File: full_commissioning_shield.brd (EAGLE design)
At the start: 140 x 53.3 mm, 118 parts, among them IC1 LSM303DLHC, IC2 TLV341A, Q1 BSS138, Q2 BSS138, Q3 NMOS BSS138, U1 ARDUINO-MEGAPRO-5V, U10 LM3405XMK, U11 DS1342U+, U13 TPS563200, U14 MIC5365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

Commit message: Fixed some errors
- Fixed a missing net
- Minor polygon fixes
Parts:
- R35: value 680k -> 580k
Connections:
- net LIGHT_PWM: now also U1.45
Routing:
- net LIGHT_PWM: track 9.08 -> 81.7 mm, vias 2 -> 3
- net SCL_3V3: track 103.5 -> 104.8 mm, vias 6 -> 5
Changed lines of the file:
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@@
 <attribute name="VALUE" x="44.7675" y="18.7325" size="1.27" layer="27"/>
 </element>
-<element name="R35" library="rcl" package="R0805" value="680k" x="45.4025" y="17.4625" smashed="yes" rot="R180">
+<element name="R35" library="rcl" package="R0805" value="580k" x="45.4025" y="17.4625" smashed="yes" rot="R180">
 <attribute name="NAME" x="42.8625" y="18.0975" size="0.8128" layer="25" rot="R270"/>
 <attribute name="VALUE" x="46.0375" y="20.0025" size="1.27" layer="27" rot="R180"/>
@@
 </element>
 <element name="C31" library="rcl" package="C0805" value="100n" x="40.9575" y="15.5575" smashed="yes" rot="R180">
-<attribute name="NAME" x="38.4175" y="16.1925" size="0.8128" layer="25" rot="R270"/>
+<attribute name="NAME" x="38.4175" y="15.875" size="0.8128" layer="25" rot="R270"/>
 <attribute name="VALUE" x="42.2275" y="18.0975" size="1.27" layer="27" rot="R180"/>
 </element>
@@
 <vertex x="27.445" y="41.25"/>
 <vertex x="21.215" y="41.25"/>
-<vertex x="21.215" y="39.6875"/>
-<vertex x="11.155" y="39.6875"/>
-<vertex x="11.155" y="45.2525"/>
-<vertex x="9.0225" y="45.2525"/>
+<vertex x="21.215" y="40.005"/>
+<vertex x="10.8375" y="40.005"/>
+<vertex x="10.8375" y="45.57"/>
+<vertex x="9.0225" y="45.57"/>
 <vertex x="9.0225" y="40.3125"/>
 <vertex x="8.9975" y="40.3125"/>
@@
 <contactref element="U10" pad="5"/>
 <contactref element="C23" pad="2"/>
-<polygon width="0.254" layer="1">
+<polygon width="0.254" layer="1" thermals="no">
 <vertex x="20.0075" y="19.9875"/>
 <vertex x="22.7925" y="19.9875"/>
@@
 <contactref element="C7" pad="1"/>
 <contactref element="R6" pad="2"/>
-<polygon width="0.254" layer="1" orphans="yes">
+<polygon width="0.254" layer="1" orphans="yes" thermals="no">
 <vertex x="18.13" y="49.6975"/>
 <vertex x="30.2775" y="49.6975"/>
@@
 <wire x1="20.3073" y1="25.6352" x2="20.3073" y2="24.5298" width="0.254" layer="1"/>
 <wire x1="20.3073" y1="24.5298" x2="20.2925" y2="24.515" width="0.254" layer="1"/>
+<contactref element="U1" pad="45"/>
+<wire x1="85.09" y1="20.32" x2="83.82" y2="19.05" width="0.3048" layer="16"/>
+<wire x1="83.82" y1="19.05" x2="40.9575" y2="19.05" width="0.3048" layer="16"/>
+<wire x1="40.9575" y1="19.05" x2="38.1" y2="16.1925" width="0.3048" layer="16"/>
+<wire x1="38.1" y1="16.1925" x2="28.8925" y2="16.1925" width="0.3048" layer="1"/>
+<wire x1="28.8925" y1="16.1925" x2="26.035" y2="19.05" width="0.3048" layer="1"/>
+<wire x1="26.035" y1="19.05" x2="18.7725" y2="19.05" width="0.3048" layer="1"/>
+<wire x1="18.7725" y1="19.05" x2="16.355" y2="21.4675" width="0.3048" layer="1"/>
+<via x="38.1" y="16.1925" extent="1-16" drill="0.35" diameter="0.1" shape="octagon"/>
 </signal>
 <signal name="N$19">
@@
 <contactref element="U10" pad="6"/>
 <contactref element="L2" pad="1"/>
-<polygon width="0.254" layer="1" rank="2">
+<polygon width="0.254" layer="1" thermals="no" rank="2">
 <vertex x="19.07" y="31.75"/>
 <vertex x="19.07" y="27.66"/>
@@
 <contactref element="L2" pad="2"/>
 <contactref element="LED" pad="1"/>
-<polygon width="0.4064" layer="1" isolate="0.3048">
+<polygon width="0.4064" layer="1" isolate="0.3048" thermals="no">
 <vertex x="15.9375" y="36.41"/>
 <vertex x="3.13" y="36.41"/>
@@
 <via x="12.7" y="25.7125" extent="1-16" drill="0.35" diameter="0.1" shape="octagon"/>
 <wire x1="12.66" y1="23.9695" x2="10.12" y2="23.9695" width="0.8128" layer="1"/>
-<polygon width="0.6096" layer="1">
+<polygon width="0.6096" layer="1" thermals="no">
 <vertex x="3.175" y="29.845"/>
 <vertex x="9.8425" y="29.845"/>
@@
 <vertex x="13.3825" y="40.625"/>
 </polygon>
-<polygon width="0.254" layer="1">
-<vertex x="11.82" y="45.3125"/>
-<vertex x="11.82" y="40.625"/>
+<polygon width="0.254" layer="1" thermals="no">
+<vertex x="11.5025" y="45.63"/>
+<vertex x="11.5025" y="40.625"/>
 <vertex x="13.07" y="40.625"/>
-<vertex x="13.07" y="45.3125"/>
+<vertex x="13.07" y="45.63"/>
 </polygon>
 <via x="12.445" y="42.1875" extent="1-16" drill="0.35" diameter="0.1" shape="octagon"/>
@@
 <wire x1="69.5325" y1="36.83" x2="68.8975" y2="37.465" width="0.254" layer="16"/>
 <contactref element="GPS" pad="14"/>
-<via x="67.5875" y="37.465" extent="1-16" drill="0.35" diameter="0.1" shape="octagon"/>
-<wire x1="67.5875" y1="37.465" x2="65.405" y2="37.465" width="0.254" layer="16"/>
+<wire x1="68.8975" y1="37.465" x2="65.405" y2="37.465" width="0.254" layer="16"/>
 <wire x1="65.405" y1="37.465" x2="63.5" y2="39.37" width="0.254" layer="16"/>
 <wire x1="63.5" y1="39.37" x2="63.5" y2="41.595" width="0.254" layer="16"/>

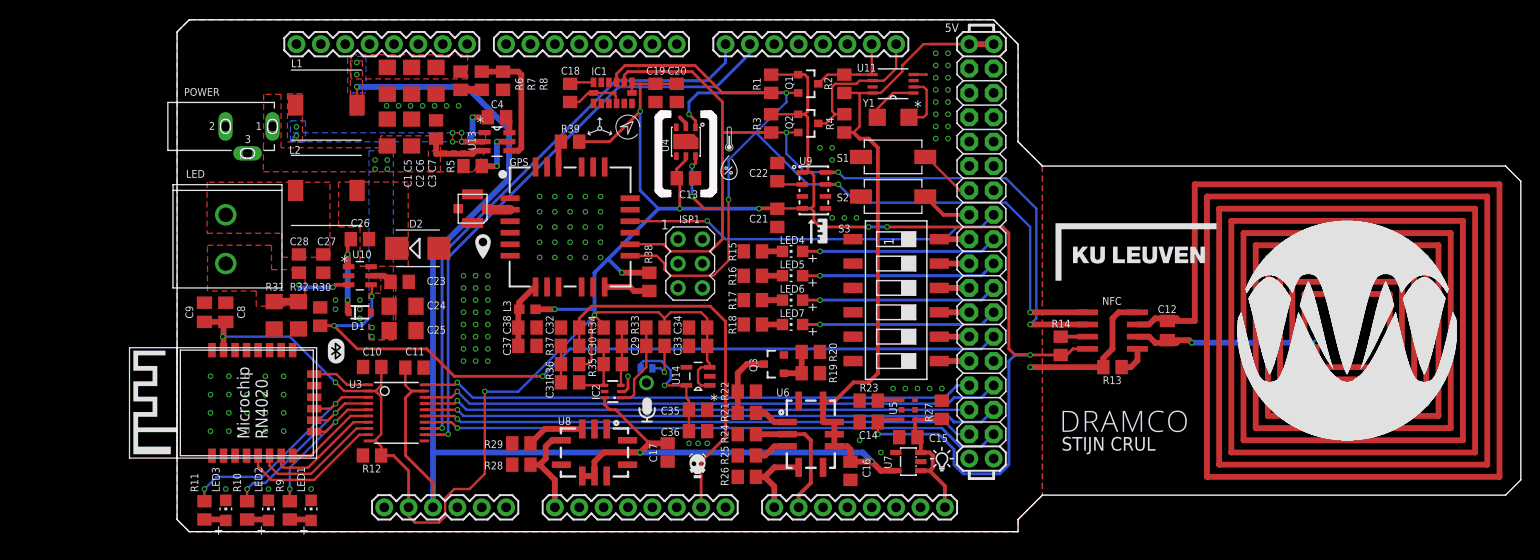
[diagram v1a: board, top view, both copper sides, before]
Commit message: Fixed footprint
Fixed Arduino Mega footprint and updated gerber files
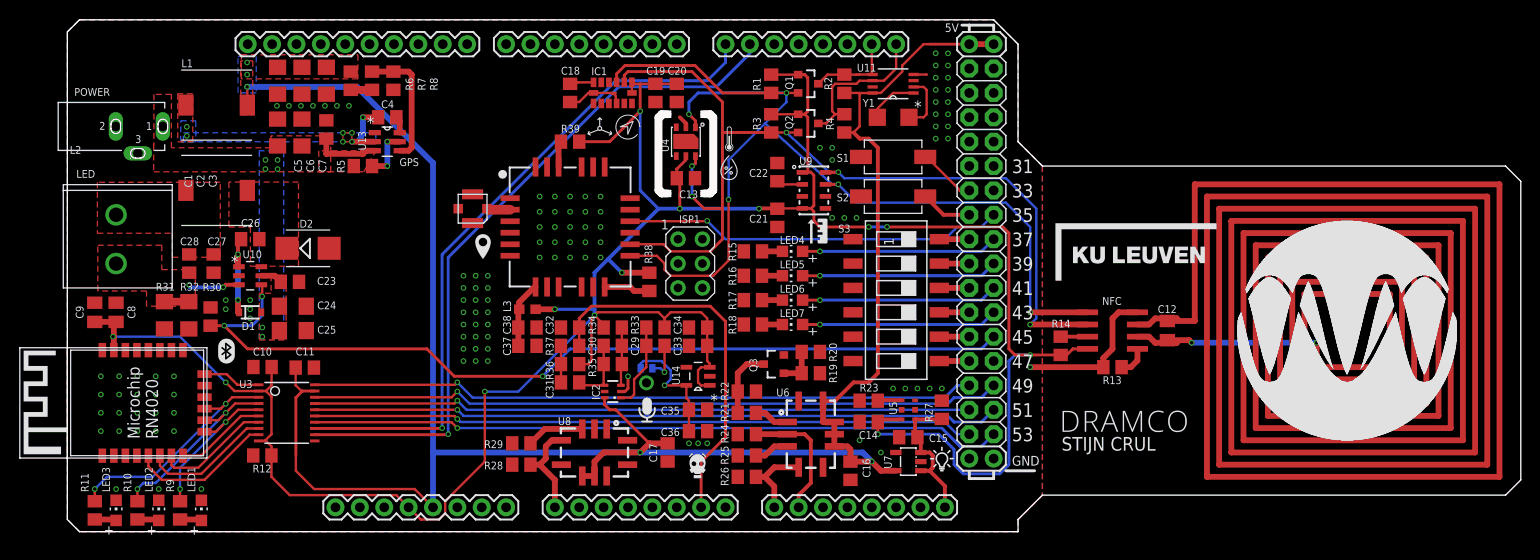
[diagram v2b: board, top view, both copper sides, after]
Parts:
- removed U1: ARDUINO-MEGAPRO-5V, SparkFun-Boards:ARDUINO_MEGA-PRO-5V
- added U12: ARDUINO-MEGAFULL, SparkFun-Boards:ARDUINO_MEGA
- moved C2 11.4 mm to (13.0, 41.6)
- moved C3 11.4 mm to (15.6, 41.9)
- moved C6 11.4 mm to (13.0, 47.0)
- moved C7 11.4 mm to (15.6, 47.0)
- moved C1 11.4 mm to (10.5, 41.6)
- moved C10 11.4 mm to (8.91, 17.2)
- moved C11 11.4 mm to (13.3, 17.1)
- moved C23 11.4 mm to (11.8, 26.0)
- moved C24 11.4 mm to (12.1, 23.5)
- moved C25 11.4 mm to (12.1, 21.0)
- moved C26 11.4 mm to (7.62, 30.5)
- moved C27 11.4 mm to (3.81, 27.9)
- moved C28 11.4 mm to (1.27, 27.9)
- moved C4 11.4 mm to (21.9, 43.2)
- moved C5 11.4 mm to (10.5, 47.0)
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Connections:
- net +3V3: now also U12.3.3V; no longer U1.3.3V
- net +5V: now also U12.5V@0, U12.5V@1, U12.5V@2; no longer U1.5V@0, U1.5V@1, U1.5V@2
- net 03: now also U12.A0; no longer U1.A0
- net ACTIVITY_ARD: now also U12.49; no longer U1.49
- net AUDIO: now also U12.A6; no longer U1.A6
- net CO: now also U12.A9; no longer U1.A9
- net CONN_ARD: now also U12.51; no longer U1.51
- net D22: now also U12.22; no longer U1.22
- net D24: now also U12.24; no longer U1.24
- net D36: now also U12.36; no longer U1.36
- net D38: now also U12.38; no longer U1.38
- net D40: now also U12.40; no longer U1.40
- net D42: now also U12.42; no longer U1.42
- net D44: now also U12.44; no longer U1.44
- net D46: now also U12.46; no longer U1.46
- net GND: now also U12.GND@0, U12.GND@1, U12.GND@2, U12.GND@3, U12.GND@4; no longer U1.GND@0, U1.GND@1, U1.GND@2, U1.GND@3, U1.GND@4
- net GPS_INT: now also U12.35; no longer U1.35
- net LED1: now also U12.37; no longer U1.37
- net LED2: now also U12.39; no longer U1.39
- net LED3: now also U12.41; no longer U1.41
- net LED4: now also U12.43; no longer U1.43
- net LIGHT_PWM: now also U12.45; no longer U1.45
- net LUX: now also U12.A15; no longer U1.A15
- net MLDPEV_ARD: now also U12.50; no longer U1.50
- net MLDP_ARD: now also U12.52; no longer U1.52
- net N$33: now also U12.25; no longer U1.25
- net NO2: now also U12.A8; no longer U1.A8
- net RX1_ARD: now also U12.19; no longer U1.19
- net RX3_ARD: now also U12.15; no longer U1.15
- net SCL_5V: now also U12.21; no longer U1.21
- net SDA_5V: now also U12.20; no longer U1.20
- net SW1: now also U12.32; no longer U1.32
- net SW2: now also U12.34; no longer U1.34
- net TX1_ARD: now also U12.18; no longer U1.18
- net TX3_ARD: now also U12.14; no longer U1.14
- net WAKEHW_ARD: now also U12.48; no longer U1.48
- net WAKESW_ARD: now also U12.53; no longer U1.53
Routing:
- net WAKESW_ARD: track 60.9 -> 72.3 mm
- net TX3_ARD: track 59.8 -> 71.2 mm
- net CONN_ARD: track 60.4 -> 71.8 mm
- net ACTIVITY_ARD: track 60.9 -> 72.3 mm
- net WAKEHW_ARD: track 58.1 -> 69.5 mm
- net RX3_ARD: track 62.1 -> 73.5 mm
- net MLDP_ARD: track 57.6 -> 69.0 mm
- net MLDPEV_ARD: track 57.3 -> 68.7 mm
- net LIGHT_PWM: track 81.7 -> 93.1 mm
- net +5V: track 215.4 -> 224.4 mm
- net +3V3: track 283.1 -> 291.7 mm
- net SCL_3V3: track 104.8 -> 103.4 mm
- net SDA_3V3: track 117.8 -> 116.4 mm
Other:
- board size 140 x 53.3 mm -> 151.4 x 53.3 mm

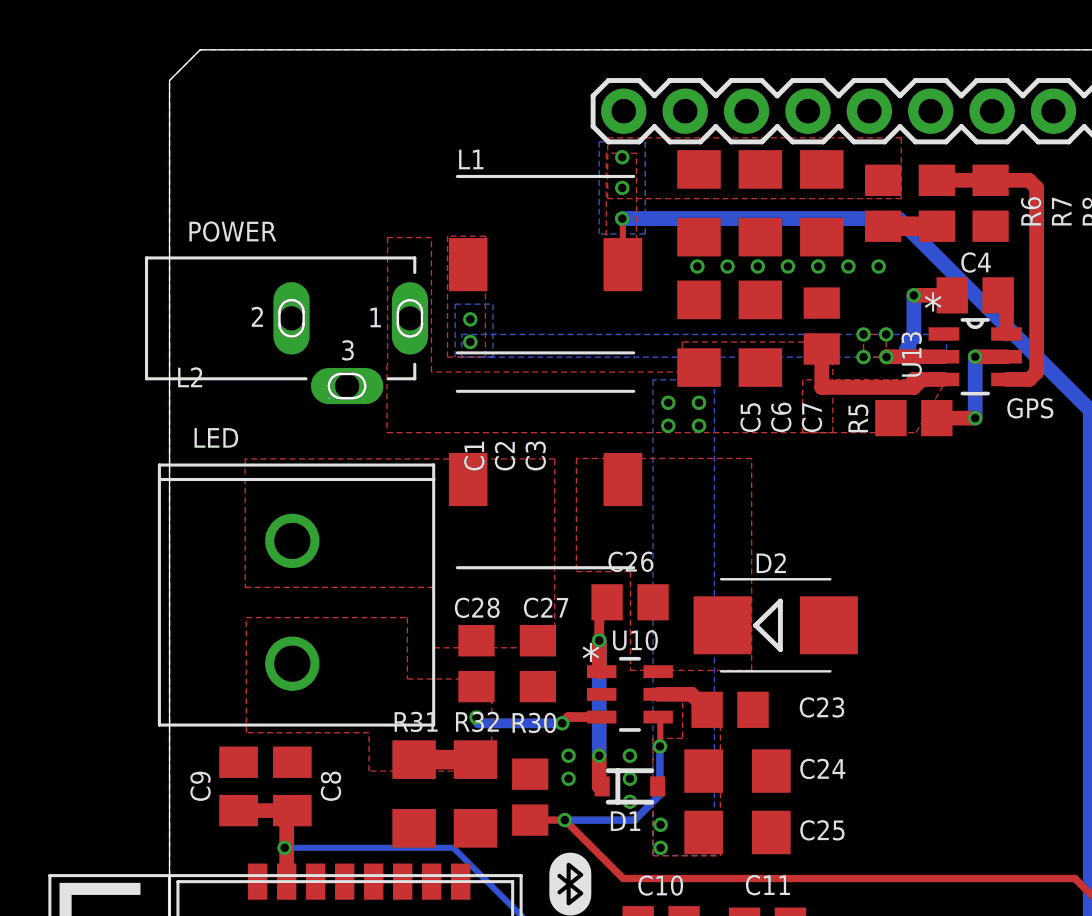
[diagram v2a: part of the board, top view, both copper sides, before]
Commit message: Minor fixes
Power connector + polygons
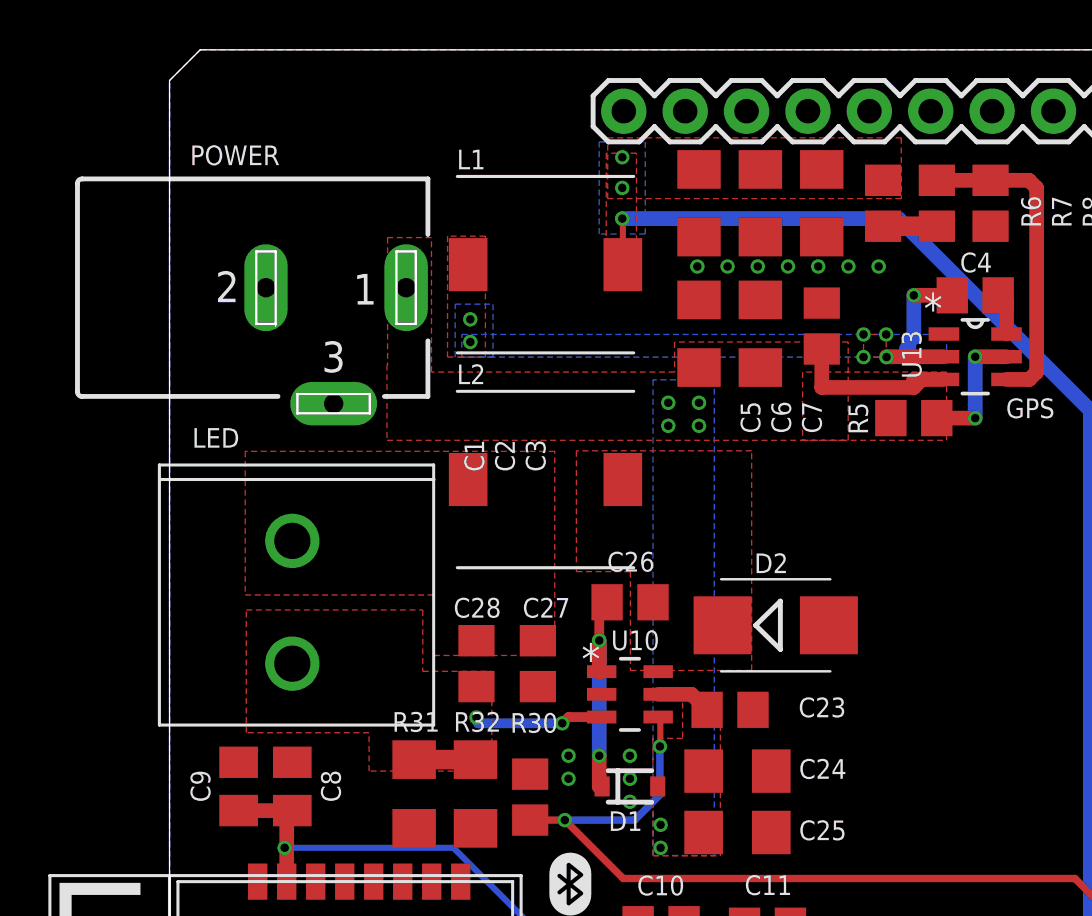
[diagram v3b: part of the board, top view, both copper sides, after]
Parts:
- POWER: device EAGLE-WR-DC_POWER_JACK_CONNECTORS-rev16b:69410X303002 -> EAGLE-WR-DC_POWER_JACK_CONNECTORS-rev17a:69410X301002
- moved POWER 3.13 mm to (-15.2, 43.5)
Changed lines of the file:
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@@
 <element name="L2" library="EagleLibrary_Wuerth_Elektronik_eiSos_rev16a" package="WE-PD_7332/7345" value="4u7, 7447789004" x="4.1275" y="35.56" smashed="yes" rot="R180">
 <attribute name="VALUE" x="7.8025" y="31.25" size="1.27" layer="27" rot="R180"/>
-<attribute name="NAME" x="-9.9775" y="40.1875" size="0.8128" layer="25" rot="R180"/>
+<attribute name="NAME" x="0.4525" y="39.505" size="0.8128" layer="25"/>
 </element>
 <element name="C23" library="rcl" package="C0805" value="100n" x="11.7625" y="26.03" smashed="yes" rot="R180">
@@
 <attribute name="VALUE" x="60.6425" y="24.13" size="1.27" layer="27" rot="R180"/>
 </element>
-<element name="POWER" library="EAGLE-WR-DC_POWER_JACK_CONNECTORS-rev16b" package="69410X303002" value="" x="-12.3825" y="42.2275" smashed="yes">
-<attribute name="NAME" x="-10.705" y="45.414" size="0.8128" layer="25" ratio="13" rot="SR0"/>
-<attribute name="VALUE" x="-9.6825" y="36.7075" size="1.27" layer="27" font="vector" ratio="13" rot="SR0"/>
-</element>
 <element name="U11" library="Maxim_By_element14_Batch_1" package="SOP65P490X110-8N" value="DS1342U+" x="74.6125" y="46.6725" smashed="yes" rot="R180">
 <attribute name="MPN" value="DS1341U+" x="74.6125" y="46.6725" size="1.778" layer="27" rot="R180" display="off"/>
@@
 </element>
 <element name="U12" library="SparkFun-Boards" package="ARDUINO_MEGA" value="ARDUINO-MEGAFULL" x="-11.43" y="0"/>
+<element name="POWER" library="EAGLE-WR-DC_POWER_JACK_CONNECTORS-rev17a" package="69410X301002" value="" x="-15.24" y="43.4975" smashed="yes">
+<attribute name="NAME" x="-10.5875" y="48.5681" size="0.8128" layer="25" ratio="13" rot="SR0"/>
+<attribute name="VALUE" x="-12.64" y="33.8491" size="2.032" layer="27" font="vector" ratio="13" rot="SR0"/>
+</element>
 </elements>
 <signals>
@@
 <contactref element="S3" pad="5"/>
 <contactref element="S3" pad="6"/>
-<contactref element="POWER" pad="2"/>
-<contactref element="POWER" pad="3"/>
 <contactref element="U11" pad="4"/>
 <contactref element="IC1" pad="7"/>
@@
 <contactref element="U12" pad="GND@2"/>
 <contactref element="U12" pad="GND@3"/>
+<contactref element="POWER" pad="2"/>
+<contactref element="POWER" pad="3"/>
 </signal>
 <signal name="INPUT">
@@
 <contactref element="C3" pad="2"/>
 <polygon width="0.254" layer="1" thermals="no">
-<vertex x="16.015" y="37.5"/>
-<vertex x="16.015" y="41.25"/>
-<vertex x="9.785" y="41.25"/>
-<vertex x="9.785" y="40.005"/>
+<vertex x="16.65" y="37.1825"/>
+<vertex x="16.65" y="41.25"/>
+<vertex x="9.4675" y="41.25"/>
+<vertex x="9.4675" y="40.005"/>
 <vertex x="-0.5925" y="40.005"/>
 <vertex x="-0.5925" y="45.57"/>
@@
 <vertex x="-2.4075" y="40.3125"/>
 <vertex x="-2.4325" y="40.3125"/>
-<vertex x="-2.4325" y="37.5"/>
+<vertex x="-2.4325" y="37.1825"/>
 </polygon>
 <polygon width="0.254" layer="1">
-<vertex x="14.765" y="37.5"/>
-<vertex x="19.4525" y="37.5"/>
-<vertex x="20.7225" y="39.6875"/>
-<vertex x="14.765" y="39.6875"/>
+<vertex x="14.765" y="37.1825"/>
+<vertex x="20.7225" y="37.1825"/>
+<vertex x="20.7225" y="40.005"/>
+<vertex x="14.765" y="40.005"/>
 </polygon>
 <wire x1="19.6977" y1="39.7002" x2="19.3675" y2="39.37" width="0.6096" layer="1"/>
 <wire x1="15.5575" y1="40.96" x2="15.5575" y2="39.37" width="0.6096" layer="1"/>
 <wire x1="15.5575" y1="39.37" x2="19.3675" y2="39.37" width="0.6096" layer="1"/>
-<contactref element="POWER" pad="1"/>
 <contactref element="D1" pad="A"/>
 <contactref element="C24" pad="1"/>
@@
 <wire x1="20.6121" y1="39.7002" x2="19.3675" y2="39.7002" width="0.6096" layer="1"/>
 <wire x1="19.3675" y1="39.7002" x2="19.3675" y2="39.37" width="0.6096" layer="1"/>
+<contactref element="POWER" pad="1"/>
 </signal>
 <signal name="N$3">
@@
 <vertex x="7.64" y="27.66"/>
 <vertex x="12.6575" y="27.66"/>
-<vertex x="12.6575" y="36.43"/>
-<vertex x="5.405" y="36.43"/>
+<vertex x="12.6575" y="36.7475"/>
+<vertex x="5.405" y="36.7475"/>
 <vertex x="5.405" y="31.75"/>
 </polygon>
@@
 <contactref element="L2" pad="2"/>
 <contactref element="LED" pad="1"/>
-<polygon width="0.4064" layer="1" isolate="0.3048" thermals="no">
-<vertex x="4.5075" y="36.41"/>
-<vertex x="-8.3" y="36.41"/>
-<vertex x="-8.3" y="31.0975"/>
-<vertex x="-0.4925" y="31.0975"/>
-<vertex x="-0.4925" y="28.5975"/>
-<vertex x="4.5075" y="28.5975"/>
+<polygon width="0.254" layer="1" thermals="no">
+<vertex x="4.5075" y="36.7275"/>
+<vertex x="-8.3" y="36.7275"/>
+<vertex x="-8.3" y="30.78"/>
+<vertex x="-0.4925" y="30.78"/>
+<vertex x="-0.4925" y="28.28"/>
+<vertex x="4.5075" y="28.28"/>
 </polygon>
 </signal>
@@
 <via x="1.27" y="25.7125" extent="1-16" drill="0.35" diameter="0.1" shape="octagon"/>
 <wire x1="1.23" y1="23.9695" x2="-1.31" y2="23.9695" width="0.8128" layer="1"/>
-<polygon width="0.6096" layer="1" thermals="no">
-<vertex x="-8.255" y="29.845"/>
-<vertex x="-1.5875" y="29.845"/>
-<vertex x="-1.5875" y="27.305"/>
-<vertex x="1.905" y="27.305"/>
+<polygon width="0.254" layer="1" thermals="no">
+<vertex x="-8.255" y="30.1625"/>
+<vertex x="-0.9525" y="30.1625"/>
+<vertex x="-0.9525" y="27.6225"/>
+<vertex x="1.905" y="27.6225"/>
 <vertex x="1.905" y="23.495"/>
 <vertex x="-3.175" y="23.495"/>
